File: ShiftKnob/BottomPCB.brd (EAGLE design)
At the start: 37.8 x 40.2 mm, 44 parts, among them IC2 7805DT, J1 AVR_SPI_PRG_6PTH, Q1 16MHz, Q2 MOSFET-NCHANNELSMD, Q3 MOSFET-PCHANNELSMD, Q4 MOSFET-NCHANNELSMD, Q5 MOSFET-NCHANNELSMD, Q6 MOSFET-NCHANNELSMD, U1 ATMEGA328, U3 FT232RL-BASICSSOP

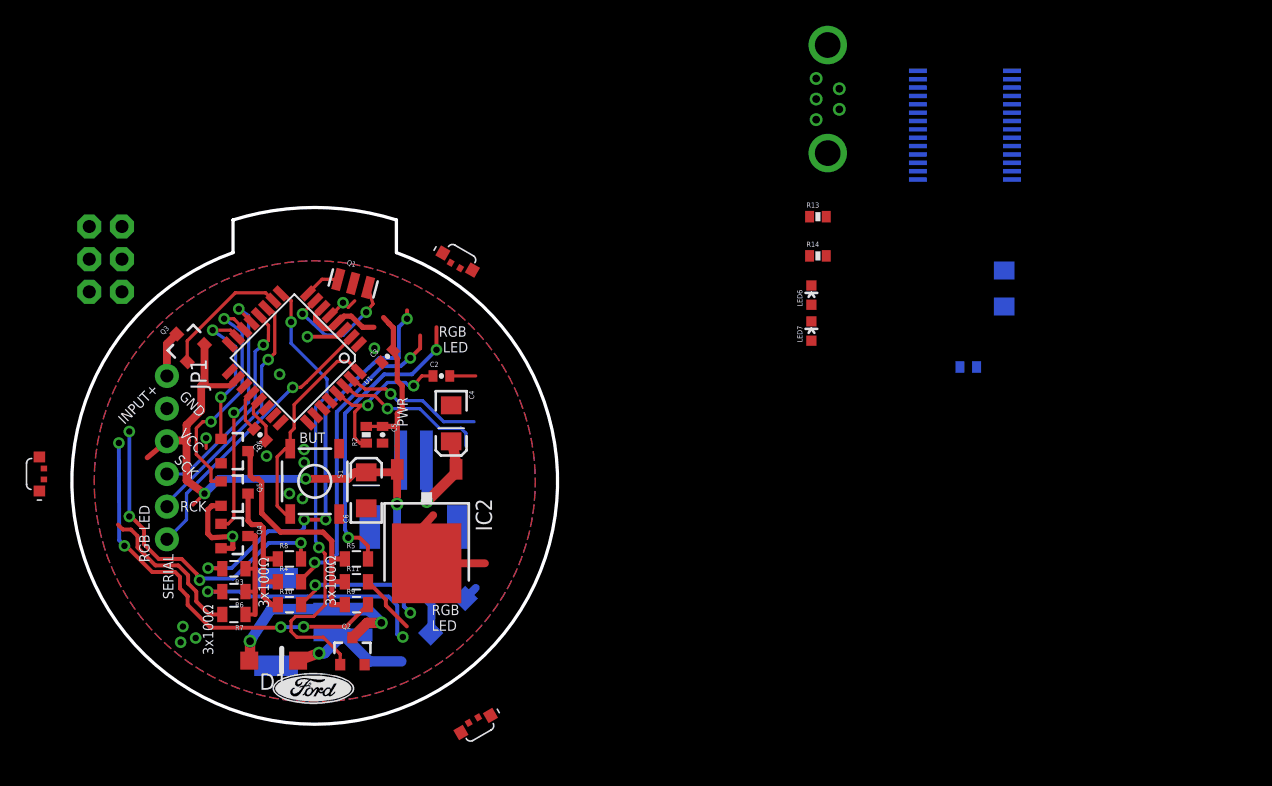
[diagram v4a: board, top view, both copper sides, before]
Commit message: add resistor arrays. clear off board layout and begin moving components.
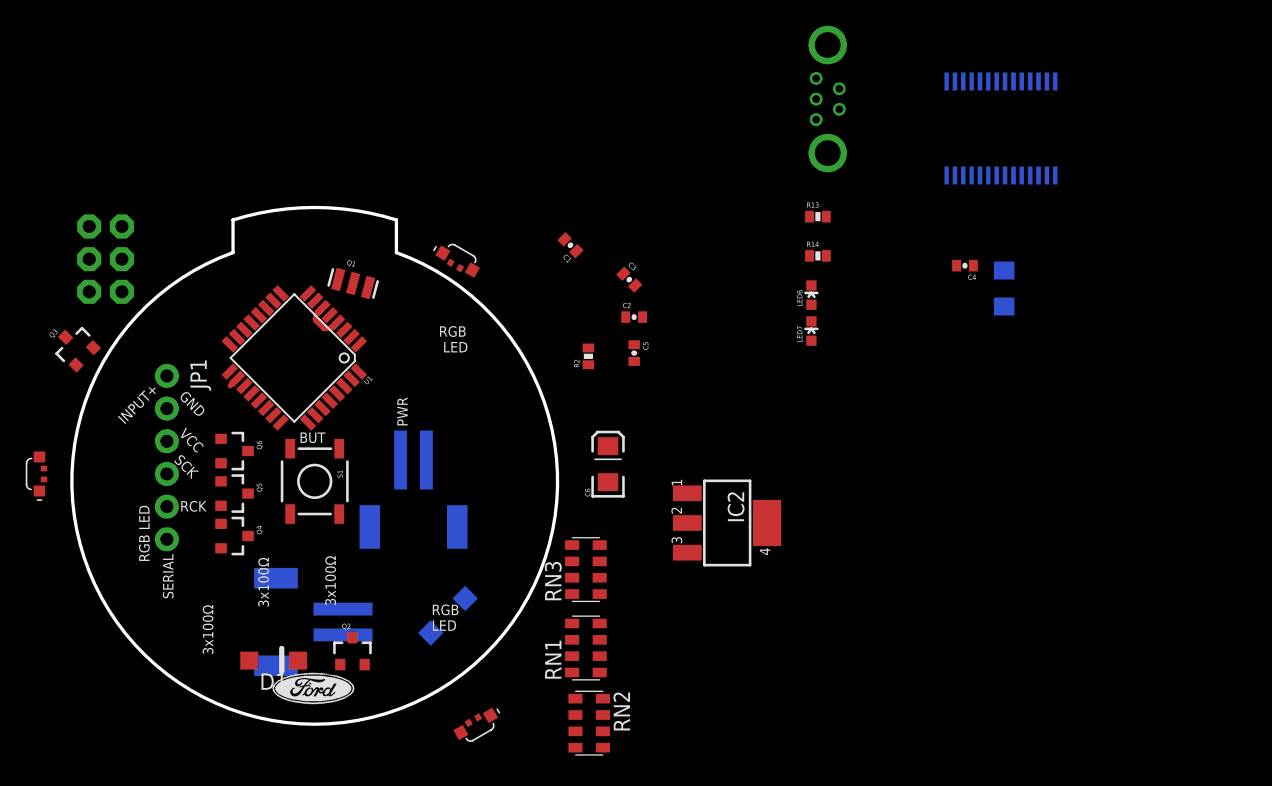
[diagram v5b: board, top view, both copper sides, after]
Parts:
- removed C9: 0.1uF, SparkFun:0402-CAP
- removed R10, R11, R3, R4, R5, R6, R7, R8, R9: 100, SparkFun-Resistors:0805
- added RN1, RN2: 150, resistor-dil:EXBS8V
- added RN3: 100, resistor-dil:EXBS8V
- C4: value 10uF -> 0.1uF; device SparkFun:EIA3216 -> SparkFun:0402-CAP
- IC2: value 7805DT -> UA78M05DCY; device linear:TO252 -> linear:SOT223
- moved U$3 62.6 mm to (80.9, 12.3)
- moved C4 41.8 mm to (72.1, 38.4), turned to 180 degrees
- moved C1 28.3 mm to (41.5, 39.9)
- moved IC2 23.4 mm to (53.7, 18.4), turned to 270 degrees
- moved C5 20.6 mm to (46.4, 31.6)
- moved C3 19.7 mm to (46.0, 37.3), turned to 315 degrees
- moved C6 18.9 mm to (44.4, 22.9)
- moved R2 18.3 mm to (42.9, 31.3)
- moved C2 15.7 mm to (46.4, 34.4)
- moved Q3 8.64 mm to (3.01, 32.0)
- moved U3 2.81 mm to (74.9, 49.0), turned to 180 degrees
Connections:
- net D10: now also RN3.1, RN3.2, RN3.3; no longer R10.1, R4.1, R8.1
- net D11: now also RN2.1, RN2.2, RN2.3; no longer R11.1, R5.1, R9.1
- net D9: now also RN1.1, RN1.2, RN1.3; no longer R3.1, R6.1, R7.1
- net GND: now also C4.1, IC2.2, IC2.4; no longer C4.C, C9.2, IC2.3
- net N$10: now also RN2.6; no longer R11.2
- net N$16: now also RN3.7; no longer R8.2
- net N$25: now also RN3.8; no longer R4.2
- net N$4: now also RN1.8; no longer R3.2
- net N$5: now also RN2.8; no longer R5.2
- net N$6: now also RN1.7; no longer R7.2
- net N$7: now also RN3.6; no longer R10.2
- net N$8: now also RN2.7; no longer R9.2
- net N$9: now also RN1.6; no longer R6.2
- net RAW: no longer C4.A
- net VCC: now also IC2.3; no longer IC2.2
- net VUSB: now also C4.2; no longer C9.1
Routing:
- net VCC: track 82.9 -> 4.34 mm, vias 4 -> 0
- net D5/MOTOR: track 35.8 -> 0.00 mm, vias 2 -> 0
- net N$4: track 32.0 -> 0.00 mm, vias 4 -> 0
- net N$8: track 31.4 -> 0.00 mm, vias 4 -> 0
- net GND: track 25.8 -> 0.00 mm, vias 14 -> 0
- net N$16: track 25.2 -> 0.00 mm, vias 4 -> 0
- net N$25: track 24.5 -> 0.00 mm, vias 2 -> 0
- net N$5: track 23.4 -> 0.00 mm, vias 2 -> 0
- net D4/SERIAL: track 22.2 -> 0.13 mm, vias 1 -> 0
- net N$11: track 20.0 -> 0.00 mm, vias 2 -> 0
- net D11: track 19.8 -> 0.00 mm
- net D7/RCK: track 19.3 -> 0.00 mm, vias 1 -> 0
- net N$9: track 19.0 -> 0.00 mm, vias 2 -> 0
- net N$12: track 18.4 -> 0.00 mm, vias 2 -> 0
- net D8/SCK: track 16.8 -> 0.00 mm, vias 1 -> 0
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- removed copper zone on layer 1, net GND
- removed copper zone on layer 16, net GND

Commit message: bring up to date. schematic almost finalized.
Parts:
- JP3: value 12V Battery Connection -> 12V Vehicle Connection
- moved D2 19.3 mm to (51.2, 9.87)
- moved R14 7.41 mm to (67.1, 35.3)
- moved LED7 4.13 mm to (63.2, 36.1)
- moved Q1 3.31 mm to (21.8, 38.8), turned to 0 degrees
- moved U1 1.93 mm to (21.8, 31.9), turned to 270 degrees
- moved JP1 1.85 mm to (10.2, 27.9)
- turned Q3 to 90 degrees
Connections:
- net RAW renamed 12V
- removed net 5V: R13.2, R14.2
- new net 3.3V: LED1.2, LED2.2, LED3.2
- net VCC: no longer LED1.2, LED2.2, LED3.2
- net VUSB: now also R13.2, R14.2
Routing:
- net VCC: track 4.34 -> 0.00 mm

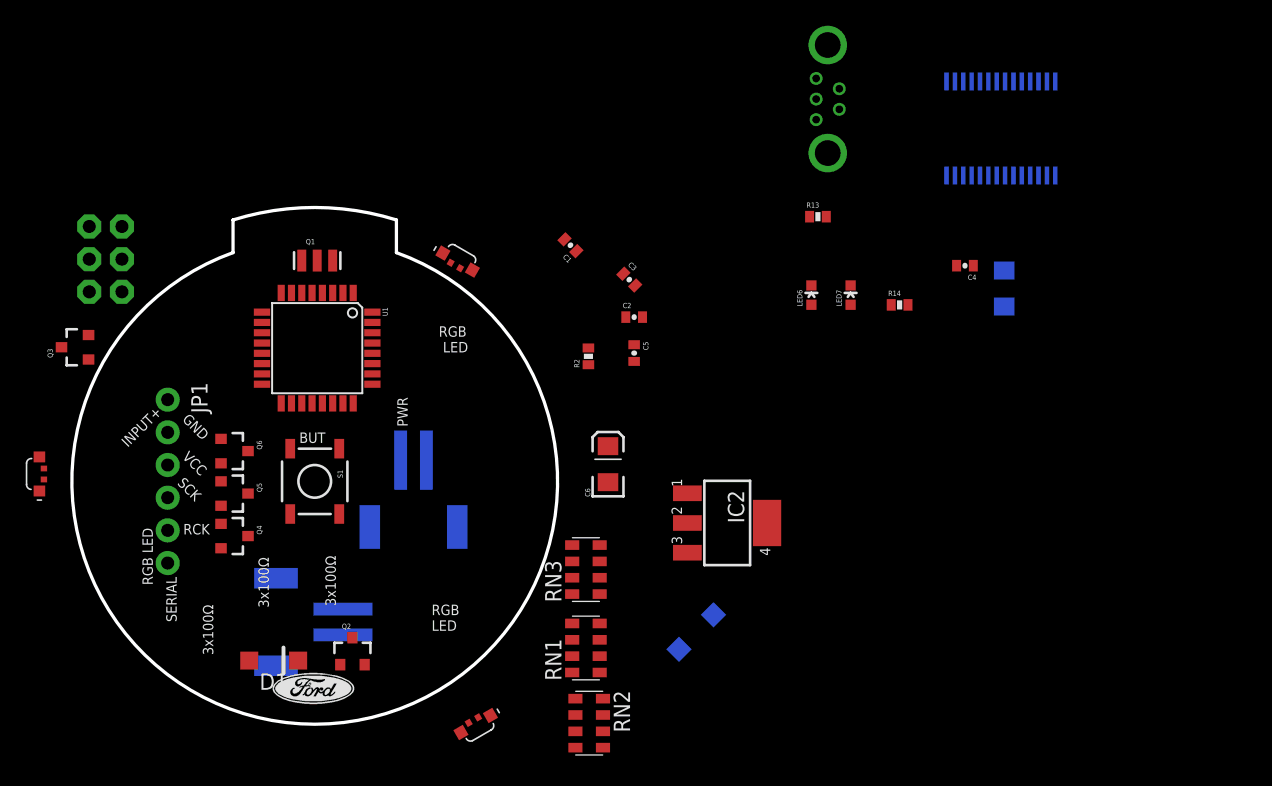
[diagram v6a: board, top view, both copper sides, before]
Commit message: add 0.1" holes in bottom PCB.
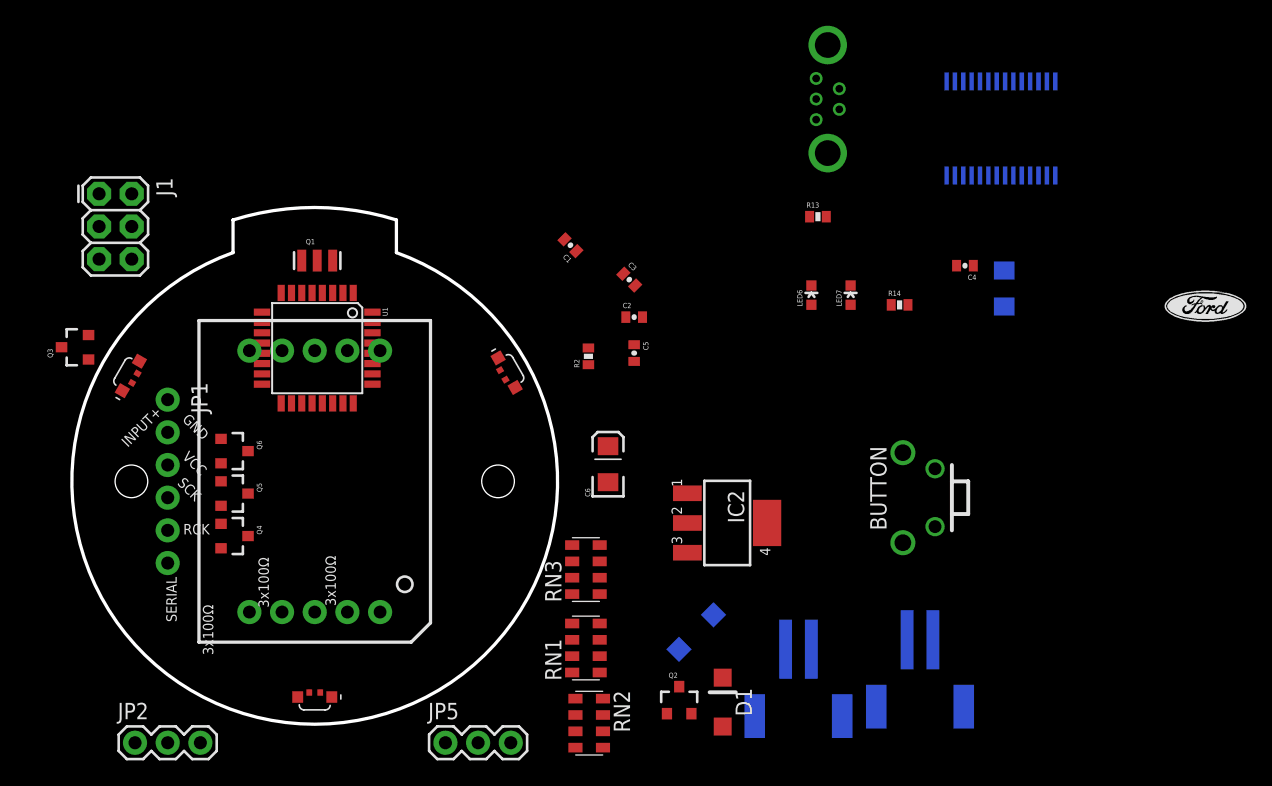
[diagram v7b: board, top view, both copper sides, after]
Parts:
- removed S1: Button, SparkFun:TACTILE_SWITCH_SMD
- added BUTTON: BUTTON_RIGHTANGLE_SMD, FORD_frames:BUTTON_RIGHTANGLE
- added JP2, JP5: (no value), SparkFun-Connectors:1X03
- added U$2: 7-SEGMENT-DISPLAY-1"-RED, SparkFun-Displays:7-SEGMENT-1"PTH
- moved JP3 41.8 mm to (68.6, 5.57)
- moved JP4 39.5 mm to (59.2, 4.84), turned to 180 degrees
- moved D1 35.1 mm to (53.3, 4.43), turned to 270 degrees
- moved Q2 25.7 mm to (49.9, 4.53)
- moved LED1 12.7 mm to (21.6, 4.83), turned to 180 degrees
- moved LED3 10.4 mm to (7.30, 29.8), turned to 60 degrees
- moved LED2 9.44 mm to (36.5, 30.0), turned to 300 degrees
- moved J1 3.10 mm to (4.83, 43.9), flipped to the top
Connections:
- new net N$20: JP2.2
- new net N$26: JP2.1
- new net N$27: JP5.3
- new net N$28: JP5.2
- new net N$29: JP5.1
- new net N$3: JP2.3
- net D2: now also BUTTON.PIN2; no longer S1.3, S1.4
- net GND: now also BUTTON.PIN1; no longer S1.1, S1.2
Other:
- board text removed: "BUT"
- board text removed: "PWR"
- board text removed: "RGB LED"
